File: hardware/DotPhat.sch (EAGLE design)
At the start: 25 parts, among them CN1 1X4-BIG, J2 RASPBERRYPI-40-PIN-GPIO_PTH, J3 USB-MICROB, U1 ATMEGA328P-MU-QFN32, U2 TMP102, X3 S4B-ZR

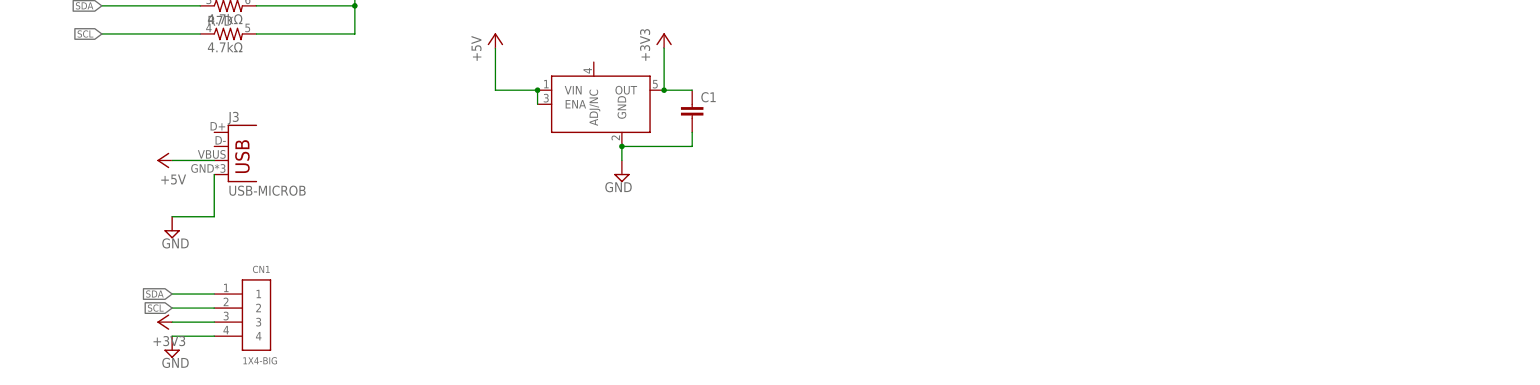
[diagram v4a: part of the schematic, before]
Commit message: Add USB programming connections
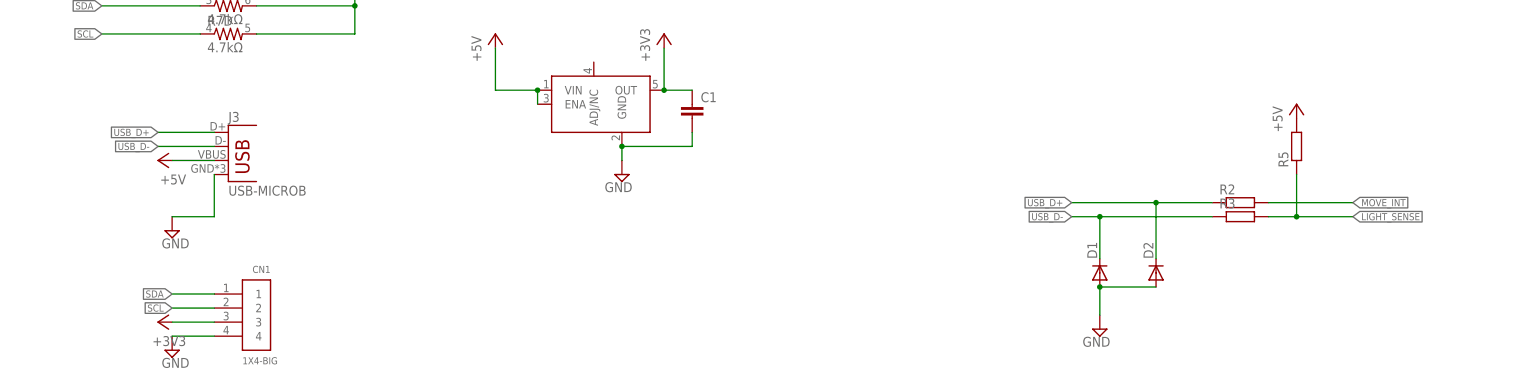
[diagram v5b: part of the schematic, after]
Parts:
- added D1, D2: (no value), diode:DIODE-SOD523
- added R2, R3, R5: (no value), rcl:R-EU_R0603
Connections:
- new net USB_D+: D2.C, J3.D+, R2.1
- new net USB_D-: D1.C, J3.D-, R3.1
- net +5V: now also R5.2
- net GND: now also D1.A, D2.A
- net LIGHT_SENSE: now also R3.2, R5.1
- net MOVE_INT: now also R2.2
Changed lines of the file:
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@@
 <part name="+3V12" library="supply1" deviceset="+3V3" device=""/>
 <part name="JP2" library="SparkFun-Jumpers" deviceset="JUMPER-SMT_3_1-NC_TRACE" device="_NO-SILK"/>
+<part name="D1" library="diode" deviceset="DIODE-" device="SOD523"/>
+<part name="D2" library="diode" deviceset="DIODE-" device="SOD523"/>
+<part name="SUPPLY14" library="supply2" deviceset="GND" device=""/>
+<part name="R2" library="rcl" deviceset="R-EU_" device="R0603"/>
+<part name="R3" library="rcl" deviceset="R-EU_" device="R0603"/>
+<part name="R5" library="rcl" deviceset="R-EU_" device="R0603"/>
+<part name="P+5" library="supply1" deviceset="+5V" device=""/>
 </parts>
 <sheets>
@@
 <instance part="+3V12" gate="G$1" x="261.62" y="10.16" rot="MR0"/>
 <instance part="JP2" gate="G$1" x="261.62" y="2.54"/>
+<instance part="D1" gate="G$1" x="236.22" y="-68.58" rot="R90"/>
+<instance part="D2" gate="G$1" x="246.38" y="-68.58" rot="R90"/>
+<instance part="SUPPLY14" gate="GND" x="236.22" y="-78.74" rot="MR0"/>
+<instance part="R2" gate="G$1" x="261.62" y="-55.88"/>
+<instance part="R3" gate="G$1" x="261.62" y="-58.42"/>
+<instance part="R5" gate="G$1" x="271.78" y="-45.72" rot="R90"/>
+<instance part="P+5" gate="1" x="271.78" y="-38.1"/>
 </instances>
 <busses>
@@
 <pinref part="JP2" gate="G$1" pin="3"/>
 </segment>
+<segment>
+<pinref part="D1" gate="G$1" pin="A"/>
+<pinref part="D2" gate="G$1" pin="A"/>
+<wire x1="236.22" y1="-71.12" x2="246.38" y2="-71.12" width="0.1524" layer="91"/>
+<pinref part="SUPPLY14" gate="GND" pin="GND"/>
+<wire x1="236.22" y1="-71.12" x2="236.22" y2="-76.2" width="0.1524" layer="91"/>
+<junction x="236.22" y="-71.12"/>
+</segment>
 </net>
 <net name="SDA" class="0">
@@
 <wire x1="27.94" y1="63.5" x2="25.4" y2="63.5" width="0.1524" layer="91"/>
 <label x="25.4" y="63.5" size="1.27" layer="95" rot="R180" xref="yes"/>
+</segment>
+<segment>
+<pinref part="R3" gate="G$1" pin="2"/>
+<wire x1="266.7" y1="-58.42" x2="271.78" y2="-58.42" width="0.1524" layer="91"/>
+<pinref part="R5" gate="G$1" pin="1"/>
+<wire x1="271.78" y1="-58.42" x2="281.94" y2="-58.42" width="0.1524" layer="91"/>
+<wire x1="271.78" y1="-50.8" x2="271.78" y2="-58.42" width="0.1524" layer="91"/>
+<junction x="271.78" y="-58.42"/>
+<label x="281.94" y="-58.42" size="1.27" layer="95" xref="yes"/>
 </segment>
 </net>
@@
 <label x="78.74" y="55.88" size="1.27" layer="95" xref="yes"/>
 </segment>
+<segment>
+<pinref part="R2" gate="G$1" pin="2"/>
+<wire x1="266.7" y1="-55.88" x2="281.94" y2="-55.88" width="0.1524" layer="91"/>
+<label x="281.94" y="-55.88" size="1.27" layer="95" xref="yes"/>
+</segment>
 </net>
 <net name="RXD" class="0">
@@
 <junction x="134.62" y="-35.56"/>
 </segment>
+<segment>
+<pinref part="R5" gate="G$1" pin="2"/>
+<pinref part="P+5" gate="1" pin="+5V"/>
+</segment>
 </net>
 <net name="N$7" class="0">
@@
 </segment>
 </net>
+<net name="USB_D-" class="0">
+<segment>
+<pinref part="J3" gate="G$1" pin="D-"/>
+<wire x1="76.2" y1="-45.72" x2="66.04" y2="-45.72" width="0.1524" layer="91"/>
+<label x="66.04" y="-45.72" size="1.27" layer="95" rot="R180" xref="yes"/>
+</segment>
+<segment>
+<pinref part="D1" gate="G$1" pin="C"/>
+<wire x1="236.22" y1="-66.04" x2="236.22" y2="-58.42" width="0.1524" layer="91"/>
+<wire x1="236.22" y1="-58.42" x2="231.14" y2="-58.42" width="0.1524" layer="91"/>
+<label x="231.14" y="-58.42" size="1.27" layer="95" rot="R180" xref="yes"/>
+<wire x1="236.22" y1="-58.42" x2="256.54" y2="-58.42" width="0.1524" layer="91"/>
+<junction x="236.22" y="-58.42"/>
+<pinref part="R3" gate="G$1" pin="1"/>
+</segment>
+</net>
+<net name="USB_D+" class="0">
+<segment>
+<pinref part="J3" gate="G$1" pin="D+"/>
+<wire x1="76.2" y1="-43.18" x2="66.04" y2="-43.18" width="0.1524" layer="91"/>
+<label x="66.04" y="-43.18" size="1.27" layer="95" rot="R180" xref="yes"/>
+</segment>
+<segment>
+<pinref part="D2" gate="G$1" pin="C"/>
+<wire x1="246.38" y1="-66.04" x2="246.38" y2="-55.88" width="0.1524" layer="91"/>
+<wire x1="246.38" y1="-55.88" x2="231.14" y2="-55.88" width="0.1524" layer="91"/>
+<label x="231.14" y="-55.88" size="1.27" layer="95" rot="R180" xref="yes"/>
+<wire x1="246.38" y1="-55.88" x2="256.54" y2="-55.88" width="0.1524" layer="91"/>
+<junction x="246.38" y="-55.88"/>
+<pinref part="R2" gate="G$1" pin="1"/>
+</segment>
+</net>

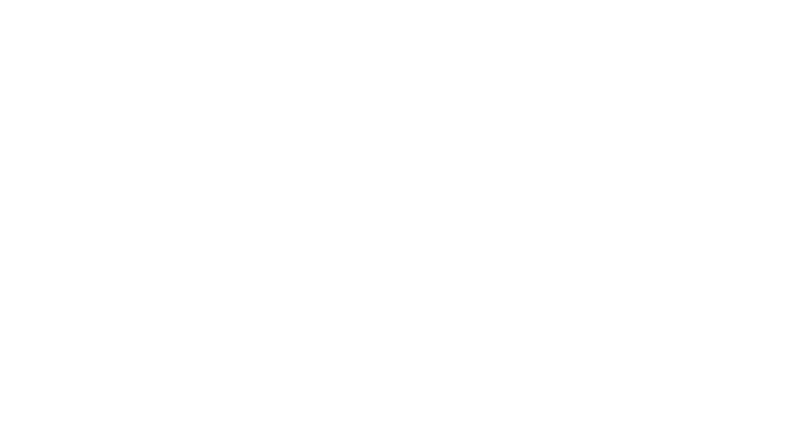
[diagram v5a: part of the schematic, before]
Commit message: Add I2C E2PROM
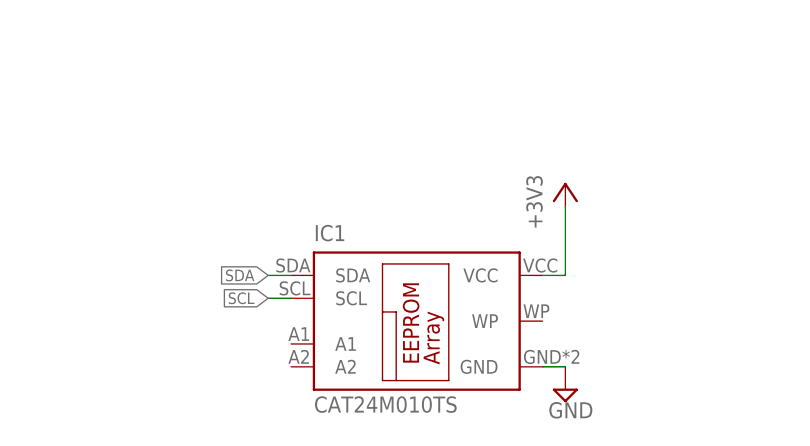
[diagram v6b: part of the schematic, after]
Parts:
- added IC1: CAT24M010TS, CAT24M01YI:CAT24M010TS
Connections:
- net +3V3: now also IC1.VCC
- net GND: now also IC1.GND
- net SCL: now also IC1.SCL
- net SDA: now also IC1.SDA
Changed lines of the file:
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@@
 <part name="R5" library="rcl" deviceset="R-EU_" device="R0603"/>
 <part name="P+5" library="supply1" deviceset="+5V" device=""/>
+<part name="SUPPLY16" library="supply2" deviceset="GND" device=""/>
+<part name="IC1" library="CAT24M01YI" deviceset="CAT24M01" device="TS" technology="0"/>
+<part name="+3V9" library="supply1" deviceset="+3V3" device=""/>
 </parts>
 <sheets>
@@
 <instance part="R5" gate="G$1" x="271.78" y="-45.72" rot="R90"/>
 <instance part="P+5" gate="1" x="271.78" y="-38.1"/>
+<instance part="SUPPLY16" gate="GND" x="111.76" y="-170.18"/>
+<instance part="IC1" gate="G$1" x="93.98" y="-162.56"/>
+<instance part="+3V9" gate="G$1" x="111.76" y="-147.32"/>
 </instances>
 <busses>
@@
 <junction x="236.22" y="-71.12"/>
 </segment>
+<segment>
+<pinref part="IC1" gate="G$1" pin="GND"/>
+<pinref part="SUPPLY16" gate="GND" pin="GND"/>
+<wire x1="109.22" y1="-167.64" x2="111.76" y2="-167.64" width="0.1524" layer="91"/>
+</segment>
 </net>
 <net name="SDA" class="0">
@@
 <wire x1="238.76" y1="12.7" x2="241.3" y2="12.7" width="0.1524" layer="91"/>
 <label x="241.3" y="12.7" size="1.27" layer="95" xref="yes"/>
+</segment>
+<segment>
+<wire x1="81.28" y1="-157.48" x2="78.74" y2="-157.48" width="0.1524" layer="91"/>
+<label x="78.74" y="-157.48" size="1.27" layer="95" rot="R180" xref="yes"/>
+<pinref part="IC1" gate="G$1" pin="SDA"/>
 </segment>
 </net>
@@
 <pinref part="JP2" gate="G$1" pin="1"/>
 </segment>
+<segment>
+<wire x1="111.76" y1="-149.86" x2="111.76" y2="-157.48" width="0.1524" layer="91"/>
+<pinref part="IC1" gate="G$1" pin="VCC"/>
+<wire x1="111.76" y1="-157.48" x2="109.22" y2="-157.48" width="0.1524" layer="91"/>
+<pinref part="+3V9" gate="G$1" pin="+3V3"/>
+</segment>
 </net>
 <net name="ADCENA" class="0">
@@
 <label x="241.3" y="10.16" size="1.27" layer="95" xref="yes"/>
 </segment>
-</net>
+<segment>
+<pinref part="IC1" gate="G$1" pin="SCL"/>
+<wire x1="81.28" y1="-160.02" x2="78.74" y2="-160.02" width="0.1524" layer="91"/>
+<label x="78.74" y="-160.02" size="1.27" layer="95" rot="R180" xref="yes"/>
+</segment>
+</net>

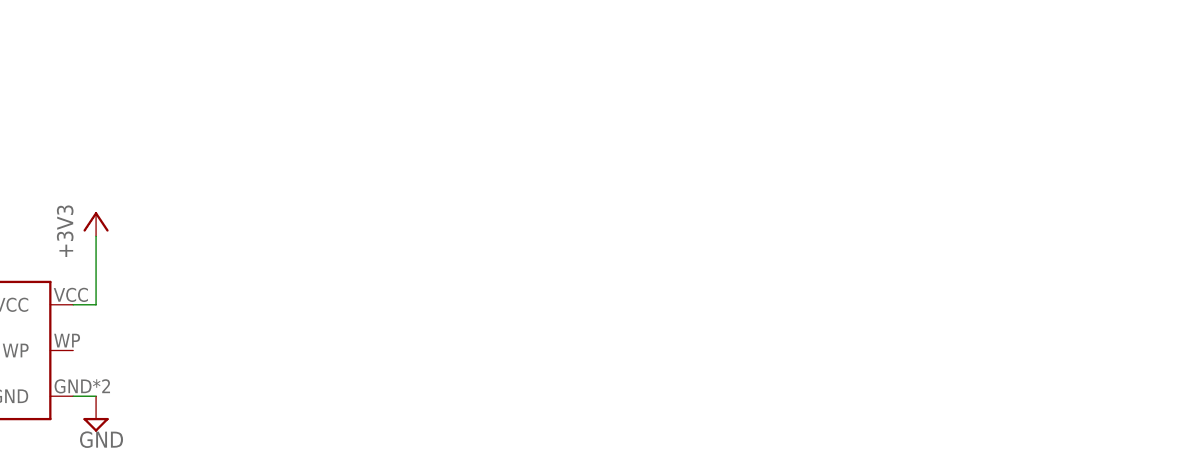
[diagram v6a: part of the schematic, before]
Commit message: Add CryptoAuthentication module
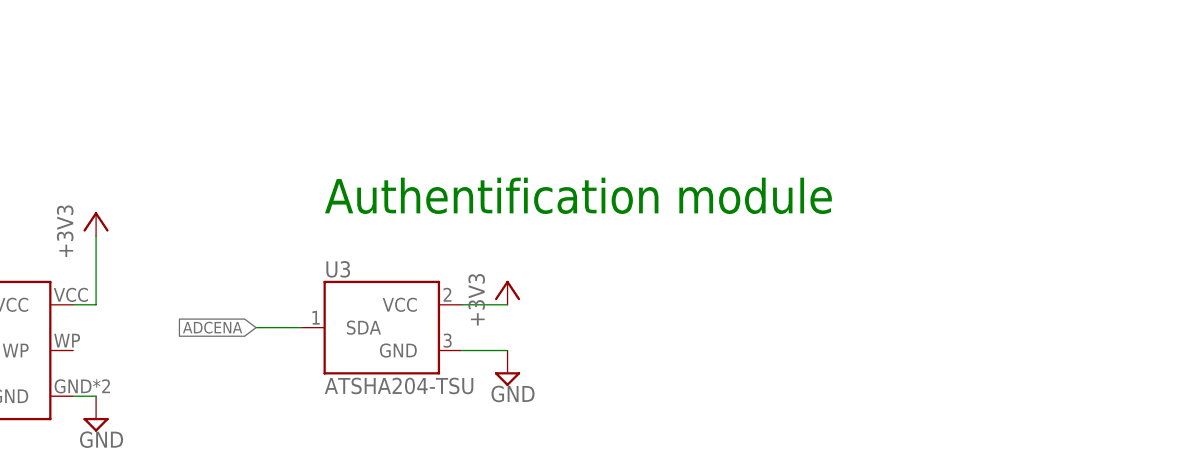
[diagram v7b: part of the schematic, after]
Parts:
- added U3: ATSHA204-TSU, SparkFun-IC-Special-Function:ATSHA204-TSU
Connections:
- net +3V3: now also U3.VCC
- net ADCENA: now also U3.SDA
- net GND: now also U3.GND
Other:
- note added: "Authentification module"
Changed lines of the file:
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@@
 <part name="IC1" library="CAT24M01YI" deviceset="CAT24M01" device="TS" technology="0"/>
 <part name="+3V9" library="supply1" deviceset="+3V3" device=""/>
+<part name="U3" library="SparkFun-IC-Special-Function" deviceset="ATSHA204" device="-TSU"/>
+<part name="+3V10" library="supply1" deviceset="+3V3" device=""/>
+<part name="SUPPLY18" library="supply2" deviceset="GND" device=""/>
 </parts>
 <sheets>
@@
 <text x="-10.922" y="50.8" size="1.27" layer="91">Red</text>
 <text x="228.6" y="20.32" size="1.016" layer="91" align="center">TMP102 or TMP112 (high acc +/-0.5°)</text>
+<text x="137.16" y="-147.32" size="3.81" layer="91">Authentification module</text>
 </plain>
 <instances>
@@
 <instance part="IC1" gate="G$1" x="93.98" y="-162.56"/>
 <instance part="+3V9" gate="G$1" x="111.76" y="-147.32"/>
+<instance part="U3" gate="G$1" x="144.78" y="-160.02"/>
+<instance part="+3V10" gate="G$1" x="157.48" y="-154.94"/>
+<instance part="SUPPLY18" gate="GND" x="157.48" y="-165.1"/>
 </instances>
 <busses>
@@
 <wire x1="109.22" y1="-167.64" x2="111.76" y2="-167.64" width="0.1524" layer="91"/>
 </segment>
+<segment>
+<pinref part="U3" gate="G$1" pin="GND"/>
+<wire x1="152.4" y1="-162.56" x2="157.48" y2="-162.56" width="0.1524" layer="91"/>
+<pinref part="SUPPLY18" gate="GND" pin="GND"/>
+</segment>
 </net>
 <net name="SDA" class="0">
@@
 <pinref part="+3V9" gate="G$1" pin="+3V3"/>
 </segment>
+<segment>
+<pinref part="U3" gate="G$1" pin="VCC"/>
+<wire x1="152.4" y1="-157.48" x2="157.48" y2="-157.48" width="0.1524" layer="91"/>
+<pinref part="+3V10" gate="G$1" pin="+3V3"/>
+</segment>
 </net>
 <net name="ADCENA" class="0">
@@
 <label x="78.74" y="86.36" size="1.27" layer="95" xref="yes"/>
 </segment>
-</net>
+<segment>
+<pinref part="U3" gate="G$1" pin="SDA"/>
+<wire x1="134.62" y1="-160.02" x2="129.54" y2="-160.02" width="0.1524" layer="91"/>
+<label x="129.54" y="-160.02" size="1.27" layer="95" rot="R180" xref="yes"/>
+</segment>
+</net>
